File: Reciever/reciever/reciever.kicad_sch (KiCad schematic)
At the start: 15 parts, among them J1 USB_C_Receptacle_USB2.0_14P, SW1 Button, SW2 Button, U1 ESP32-C6-WROOM-1, U3 SE5218ALG-LF

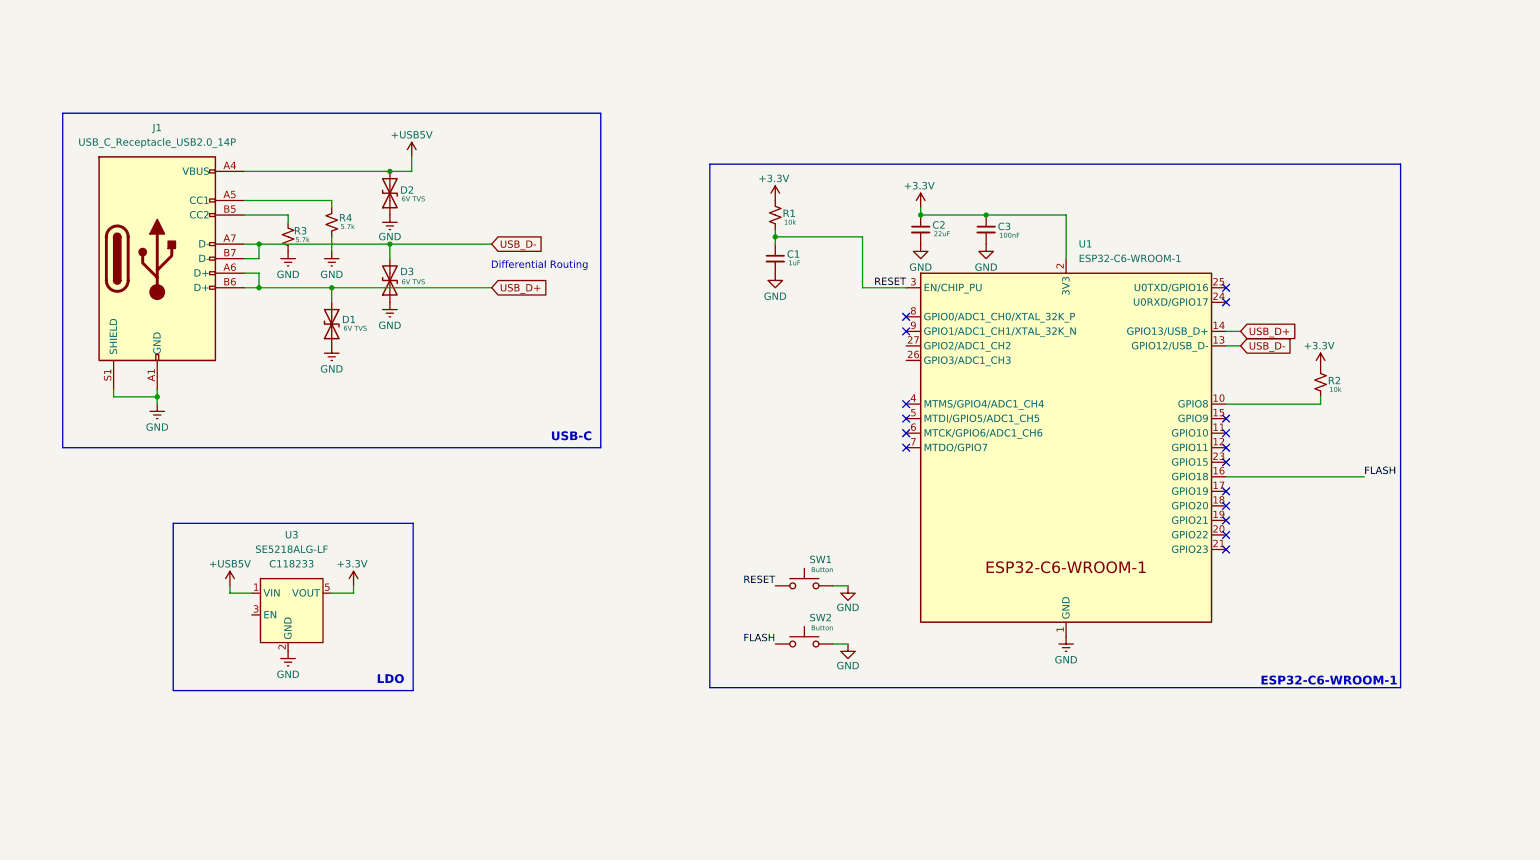
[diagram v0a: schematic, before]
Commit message: crc v1
board finished and ready for assembly setup!
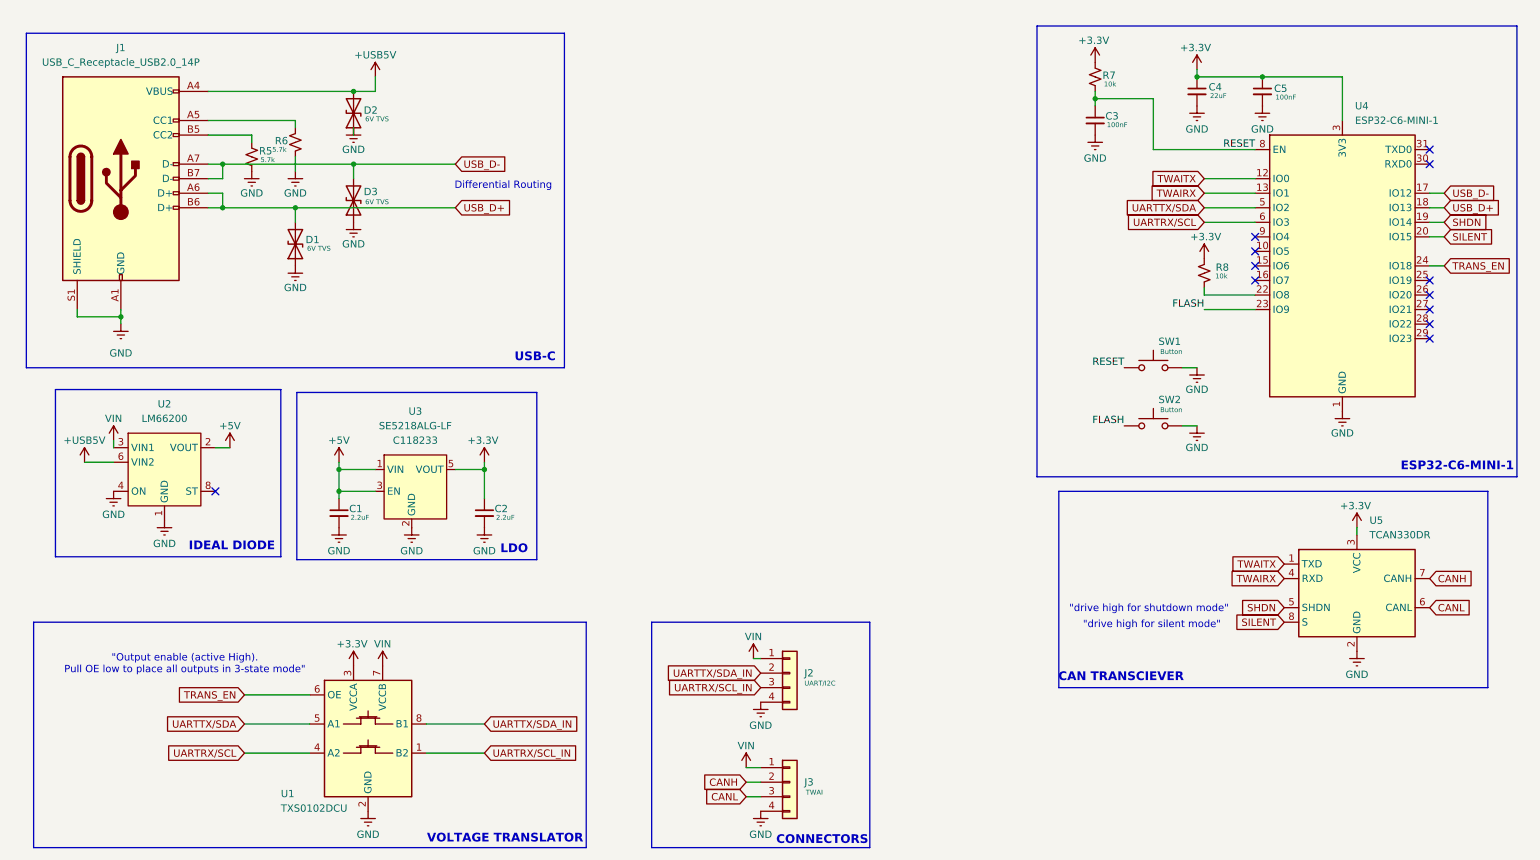
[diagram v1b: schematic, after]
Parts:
- removed R1, R2: 10k, Resistor_SMD:R_0402_1005Metric, symbol Device:R_Small_US
- removed R3, R4: 5.7k, Resistor_SMD:R_0402_1005Metric, symbol Device:R_Small_US
- removed U1: ESP32-C6-WROOM-1, RF_Module:ESP32-C6-MINI-1, symbol PCM_Espressif:ESP32-C6-WROOM-1
- added C4: 22uF, Capacitor_SMD:C_0805_2012Metric, symbol Device:C_Small
- added C5: 100nF, Capacitor_SMD:C_0402_1005Metric, symbol Device:C_Small
- added J2: UART/I2C, footprints:CONN-SMD_PH2.0-4PWB, symbol Connector_Generic:Conn_01x04
- added J3: TWAI, footprints:CONN-SMD_PH2.0-4PWB, symbol Connector_Generic:Conn_01x04
- added R5, R6: 5.7k, Resistor_SMD:R_0402_1005Metric, symbol Device:R_Small_US
- added R7, R8: 10k, Resistor_SMD:R_0402_1005Metric, symbol Device:R_Small_US
- added U1: TXS0102DCU, Package_SO:VSSOP-8_2.3x2mm_P0.5mm, symbol Logic_LevelTranslator:TXS0102DCU
- added U2: LM66200, Package_TO_SOT_SMD:SOT-583-8, symbol components:LM66200
- added U4: ESP32-C6-MINI-1, RF_Module:ESP32-C6-MINI-1, symbol RF_Module:ESP32-C6-MINI-1
- added U5: TCAN330DR, Package_SO:SOIC-8-1EP_3.9x4.9mm_P1.27mm_EP2.29x3mm, symbol Interface_CAN_LIN:TCAN330
- C1: value 1uF -> 2.2uF; footprint Capacitor_SMD:C_0805_2012Metric -> Capacitor_SMD:C_0402_1005Metric; LCSC# C380337 -> C338067
- C2: value 22uF -> 2.2uF; footprint Capacitor_SMD:C_0805_2012Metric -> Capacitor_SMD:C_0402_1005Metric; LCSC# C380337 -> C338067
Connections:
- net +3.3V: now also C4.1, C5.1, R7.1, R8.1, U1.3 (VCCA), U4.3 (3V3), U5.3 (VCC); no longer C3.1
- net +USB5V: now also U2.6 (VIN2); no longer U3.1 (VIN)
- net FLASH: now also U4.23 (IO9)
- net GND: now also C4.2, C5.2, J2.4 (Pin_4), J3.4 (Pin_4), R5.2, R6.2, U1.2 (GND), U2.1 (GND), U2.4 (ON), U2.5 (GND), U4.1 (GND), U4.11 (GND), U4.14 (GND), U4.2 (GND), U4.36 (GND), U4.37 (GND), U4.38 (GND), U4.39 (GND), U4.40 (GND), U4.41 (GND), U4.42 (GND), U4.43 (GND), U4.44 (GND), U4.45 (GND), U4.46 (GND), U4.47 (GND), U4.48 (GND), U4.49 (GND), U4.50 (GND), U4.51 (GND), U4.52 (GND), U4.53 (GND), U5.2 (GND)
- net RESET: now also C3.1, R7.2, U4.8 (EN); no longer C1.1
- net USB_D+: now also U4.18 (IO13)
- net USB_D-: now also U4.17 (IO12)
- net +5V: now reaches U3.3 (EN)
- net +5V: now also C1.1, U3.1 (VIN), U2.2 (VOUT), U2.7 (VOUT)
- net at J1.A5 (CC1): now also R6.1
- net at J1.B5 (CC2): now also R5.1
- new net: R8.2, U4.22 (IO8)
- new net CANH: J3.2 (Pin_2), U5.7 (CANH)
- new net CANL: J3.3 (Pin_3), U5.6 (CANL)
- new net SHDN: U4.19 (IO14), U5.5 (SHDN)
- new net SILENT: U4.20 (IO15), U5.8 (S)
- new net TRANS_EN: U1.6 (OE), U4.24 (IO18)
- new net TWAIRX: U4.13 (IO1), U5.4 (RXD)
- new net TWAITX: U4.12 (IO0), U5.1 (TXD)
- new net UARTRX/SCL: U1.4 (A2), U4.6 (IO3)
- new net UARTRX/SCL_IN: J2.3 (Pin_3), U1.1 (B2)
- new net UARTTX/SDA: U1.5 (A1), U4.5 (IO2)
- new net UARTTX/SDA_IN: J2.2 (Pin_2), U1.8 (B1)
- new net VIN: J2.1 (Pin_1), J3.1 (Pin_1), U1.7 (VCCB), U2.3 (VIN1)
- no-connect marks 17 -> 12
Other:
- note added: ""Output enable (active High). Pull OE low to place all outputs in 3-state mode""
- note added: ""drive high for shutdown mode""
- note added: ""drive high for silent mode""
- note added: "CAN TRANSCIEVER"
- note added: "CONNECTORS"
- note added: "ESP32-C6-MINI-1"
- note added: "IDEAL DIODE"
- note added: "VOLTAGE TRANSLATOR"
- note removed: "ESP32-C6-WROOM-1"
- moved on the sheet: U3

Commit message: crc v1
quick fixes
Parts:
- R5, R6: value 5.7k -> 5.1k
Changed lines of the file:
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@@
 			)
 		)
-		(property "Value" "5.7k"
+		(property "Value" "5.1k"
 			(at 62.484 38.608 0)
 			(effects
@@
 		(dnp no)
 		(property "Reference" "R6"
-			(at 67.31 35.306 0)
+			(at 72.39 35.306 0)
 			(effects
 				(font
@@
 			)
 		)
-		(property "Value" "5.7k"
-			(at 67.056 36.83 0)
-			(effects
-				(font
+		(property "Value" "5.1k"
+			(at 72.644 36.83 0)
+			(effects
+				(font

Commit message: crc v2
finalizing receiver layout
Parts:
- added D4, D5: D_Schottky, Diode_SMD:D_SOD-123, symbol Device:D_Schottky
- U2: LCSC# (none) -> C3235556
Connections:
- net GND: now also D4.2 (A), D5.2 (A)
- net VIN: now also D4.1 (K), D5.1 (K)
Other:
- moved on the sheet: C1, C2, D1, D2, D3, J1, J2, J3, R5, R6, U2, U3

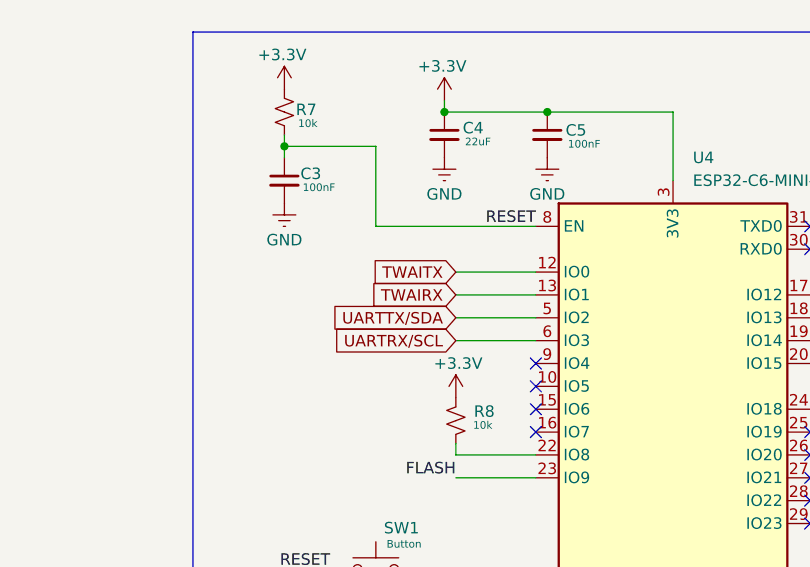
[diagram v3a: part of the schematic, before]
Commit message: crc v2
main board and receiver finalized. ready for assembly!
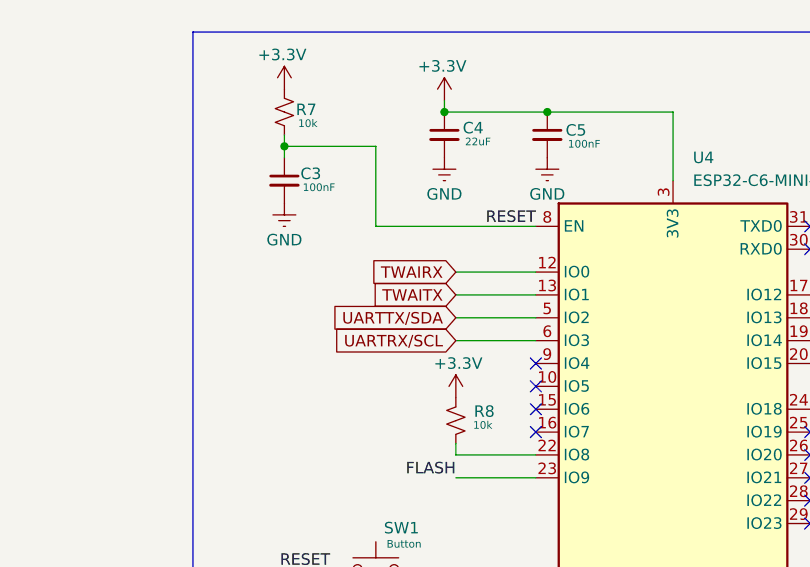
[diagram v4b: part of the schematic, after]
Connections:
- net TWAIRX: now also U4.12 (IO0); no longer U4.13 (IO1)
- net TWAITX: now also U4.13 (IO1); no longer U4.12 (IO0)

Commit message: crc v2
remote and receiver complete! assembly and orders have been prepared for purchasing.
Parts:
- C1, C2: MPN (none) -> C338067
- C3, C5: MPN (none) -> C22435938
- C4: MPN (none) -> C380337
- D1, D2, D3: MPN (none) -> C316043
- D4, D5: MPN (none) -> C41376455
- J1: MPN (none) -> C165948
- J2, J3: MPN (none) -> C50137
- R5, R6: MPN (none) -> C852861
- R7, R8: MPN (none) -> C190095
- SW1, SW2: MPN (none) -> C720477
- U1: MPN (none) -> C53434
- U2: MPN (none) -> C3235556
- U3: MPN (none) -> C118233
- U4: LCSC# (none) -> C5736265; MPN (none) -> C5736265
- U5: MPN (none) -> C2652876
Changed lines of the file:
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@@
 			)
 		)
+		(property "MPN" "C720477"
+			(at 218.44 85.09 0)
+			(effects
+				(font
+					(size 1.27 1.27)
+				)
+				(hide yes)
+			)
+		)
 		(pin "2"
 		)
@@
 			)
 		)
+		(property "MPN" "C316043"
+			(at 82.55 41.91 0)
+			(effects
+				(font
+					(size 1.27 1.27)
+				)
+				(hide yes)
+			)
+		)
 		(pin "1"
 		)
@@
 			)
 		)
+		(property "MPN" "C380337"
+			(at 226.06 26.67 0)
+			(effects
+				(font
+					(size 1.27 1.27)
+				)
+				(hide yes)
+			)
+		)
 		(pin "2"
 		)
@@
 			)
 		)
+		(property "MPN" "C53434"
+			(at 81.28 139.7 0)
+			(effects
+				(font
+					(size 1.27 1.27)
+				)
+				(hide yes)
+			)
+		)
 		(pin "2"
 		)
@@
 			)
 		)
+		(property "MPN" "C50137"
+			(at 161.29 147.32 0)
+			(effects
+				(font
+					(size 1.27 1.27)
+				)
+				(hide yes)
+			)
+		)
 		(pin "2"
 		)
@@
 			)
 		)
+		(property "MPN" "C22435938"
+			(at 237.49 26.67 0)
+			(effects
+				(font
+					(size 1.27 1.27)
+				)
+				(hide yes)
+			)
+		)
 		(pin "2"
 		)
@@
 			)
 		)
+		(property "MPN" "C41376455"
+			(at 135.89 148.59 0)
+			(effects
+				(font
+					(size 1.27 1.27)
+				)
+				(hide yes)
+			)
+		)
 		(pin "1"
 		)
@@
 			)
 		)
+		(property "MPN" "C852861"
+			(at 64.77 34.29 0)
+			(effects
+				(font
+					(size 1.27 1.27)
+				)
+				(hide yes)
+			)
+		)
 		(pin "1"
 		)
@@
 			)
 		)
+		(property "MPN" "C316043"
+			(at 72.39 49.53 0)
+			(effects
+				(font
+					(size 1.27 1.27)
+				)
+				(hide yes)
+			)
+		)
 		(pin "1"
 		)
@@
 			)
 		)
+		(property "MPN" "C2652876"
+			(at 254 114.3 0)
+			(effects
+				(font
+					(size 1.27 1.27)
+				)
+				(hide yes)
+			)
+		)
 		(pin "8"
 		)
@@
 			)
 		)
+		(property "MPN" "C22435938"
+			(at 208.28 31.75 0)
+			(effects
+				(font
+					(size 1.27 1.27)
+				)
+				(hide yes)
+			)
+		)
 		(pin "2"
 		)
@@
 			)
 		)
+		(property "MPN" "C720477"
+			(at 218.44 74.93 0)
+			(effects
+				(font
+					(size 1.27 1.27)
+				)
+				(hide yes)
+			)
+		)
 		(pin "2"
 		)
@@
 			)
 		)
+		(property "LCSC#" "C5736265"
+			(at 251.46 57.15 0)
+			(effects
+				(font
+					(size 1.27 1.27)
+				)
+				(hide yes)
+			)
+		)
+		(property "MPN" "C5736265"
+			(at 251.46 57.15 0)
+			(effects
+				(font
+					(size 1.27 1.27)
+				)
+				(hide yes)
+			)
+		)
 		(pin "42"
 		)
@@
 			)
 		)
+		(property "MPN" "C118233"
+			(at 96.52 92.71 0)
+			(effects
+				(font
+					(size 1.27 1.27)
+				)
+				(hide yes)
+			)
+		)
 		(pin "1"
 		)
@@
 			)
 		)
+		(property "MPN" "C3235556"
+			(at 44.45 90.17 0)
+			(effects
+				(font
+					(size 1.27 1.27)
+				)
+				(hide yes)
+			)
+		)
 		(pin "2"
 		)
@@
 			)
 		)
+		(property "MPN" "C190095"
+			(at 208.28 24.13 0)
+			(effects
+				(font
+					(size 1.27 1.27)
+				)
+				(hide yes)
+			)
+		)
 		(pin "1"
 		)
@@
 			)
 		)
+		(property "MPN" "C852861"
+			(at 72.39 31.75 0)
+			(effects
+				(font
+					(size 1.27 1.27)
+				)
+				(hide yes)
+			)
+		)
 		(pin "1"
 		)
@@
 			)
 		)
+		(property "MPN" "C165948"
+			(at 41.91 38.1 0)
+			(effects
+				(font
+					(size 1.27 1.27)
+				)
+				(hide yes)
+			)
+		)
 		(pin "A7"
 		)
@@
 			)
 		)
+		(property "MPN" "C316043"
+			(at 82.55 26.67 0)
+			(effects
+				(font
+					(size 1.27 1.27)
+				)
+				(hide yes)
+			)
+		)
 		(pin "1"
 		)
@@
 			)
 		)
+		(property "MPN" "C41376455"
+			(at 128.27 129.54 0)
+			(effects
+				(font
+					(size 1.27 1.27)
+				)
+				(hide yes)
+			)
+		)
 		(pin "1"
 		)
@@
 			)
 		)
+		(property "MPN" "C50137"
+			(at 161.29 128.27 0)
+			(effects
+				(font
+					(size 1.27 1.27)
+				)
+				(hide yes)
+			)
+		)
 		(pin "2"
 		)
@@
 			)
 		)
+		(property "MPN" "C190095"
+			(at 227.33 58.42 0)
+			(effects
+				(font
+					(size 1.27 1.27)
+				)
+				(hide yes)
+			)
+		)
 		(pin "1"
 		)
@@
 			)
 		)
+		(property "MPN" "C338067"
+			(at 109.22 97.79 0)
+			(effects
+				(font
+					(size 1.27 1.27)
+				)
+				(hide yes)
+			)
+		)
 		(pin "2"
 		)
@@
 			(at 83.82 97.79 0)
 			(effects
+				(font
+					(size 1.27 1.27)
+				)
+				(hide yes)
+			)
+		)
+		(property "MPN" "C338067"
+			(at 83.82 97.79 0)
+			(effects

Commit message: Custom RC V2
Final Remote + Receiver!

Special thanks to the CRCW25 Electrical Team who contributed to its development!

Jun
Katie
Nelson
David
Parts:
- removed D4, D5: D_Schottky, Diode_SMD:D_SOD-123, symbol Device:D_Schottky
- added D4, D5: 15V TVS, Diode_SMD:D_0402_1005Metric, symbol Device:D_TVS
- D1, D2, D3: value 6V TVS -> 15V TVS
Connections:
- net GND: now also D4.1 (A1), D5.1 (A1)
- net VIN: now also D4.2 (A2), D5.2 (A2)
